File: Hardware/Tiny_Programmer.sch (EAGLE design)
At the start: 31 parts, among them Q1 16MHz, U1 ATTINY84, X1 USB-A-H

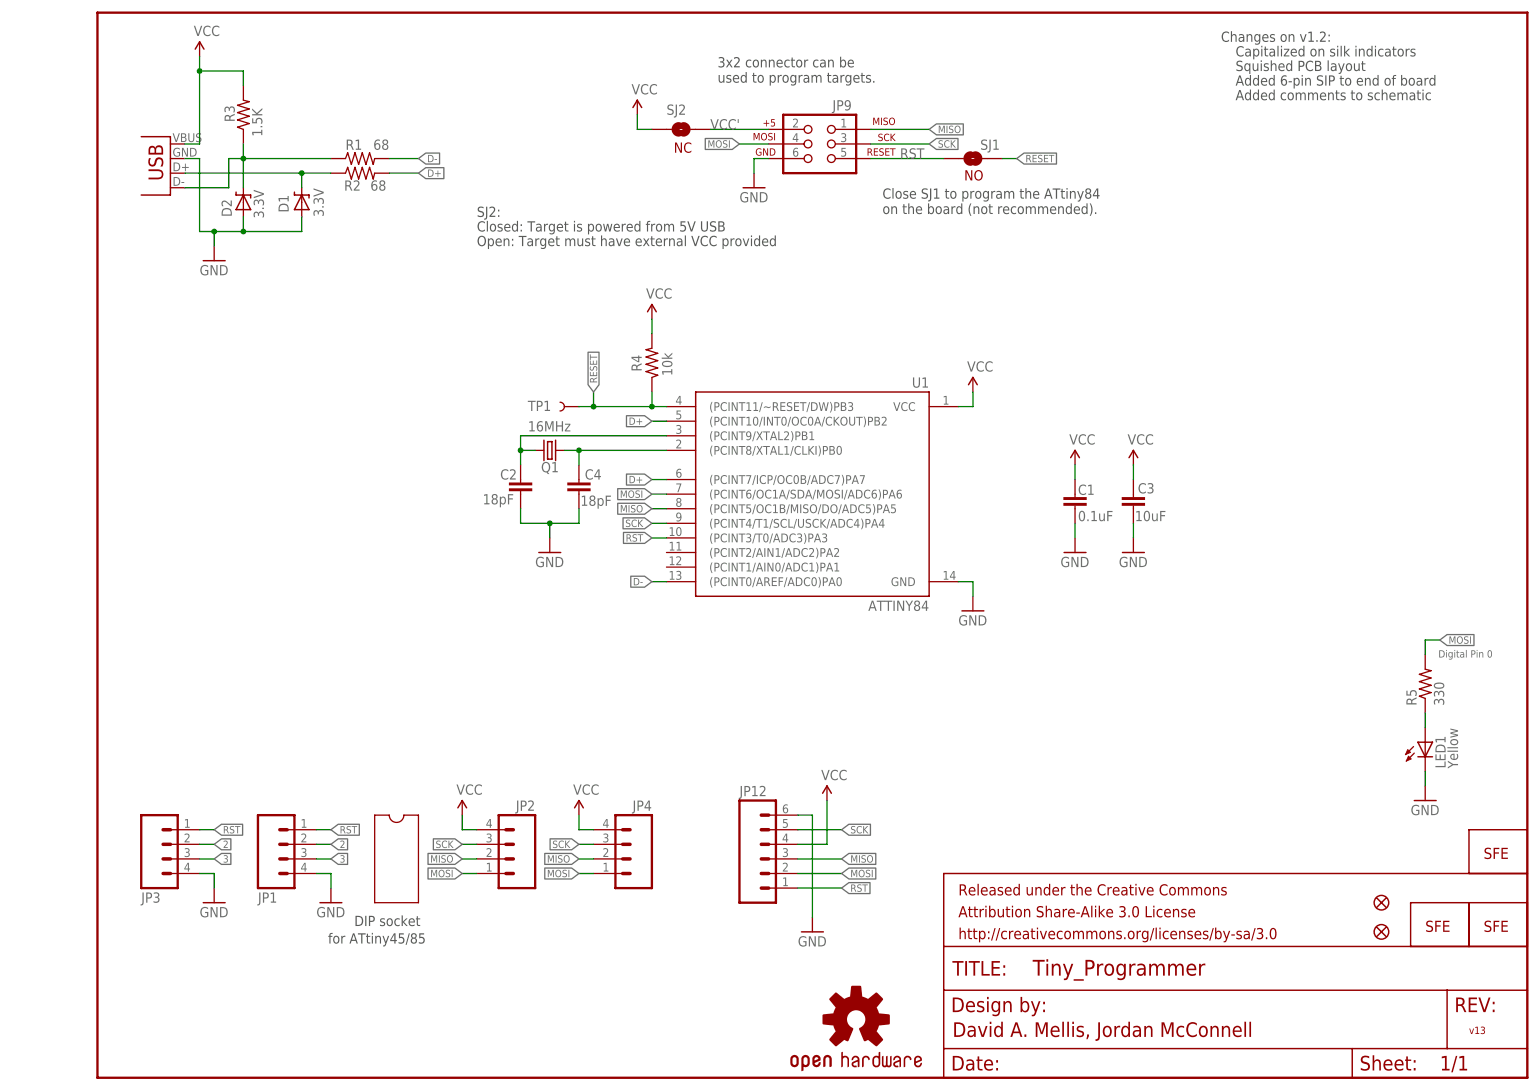
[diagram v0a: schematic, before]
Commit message: replace USB port, and redraw board
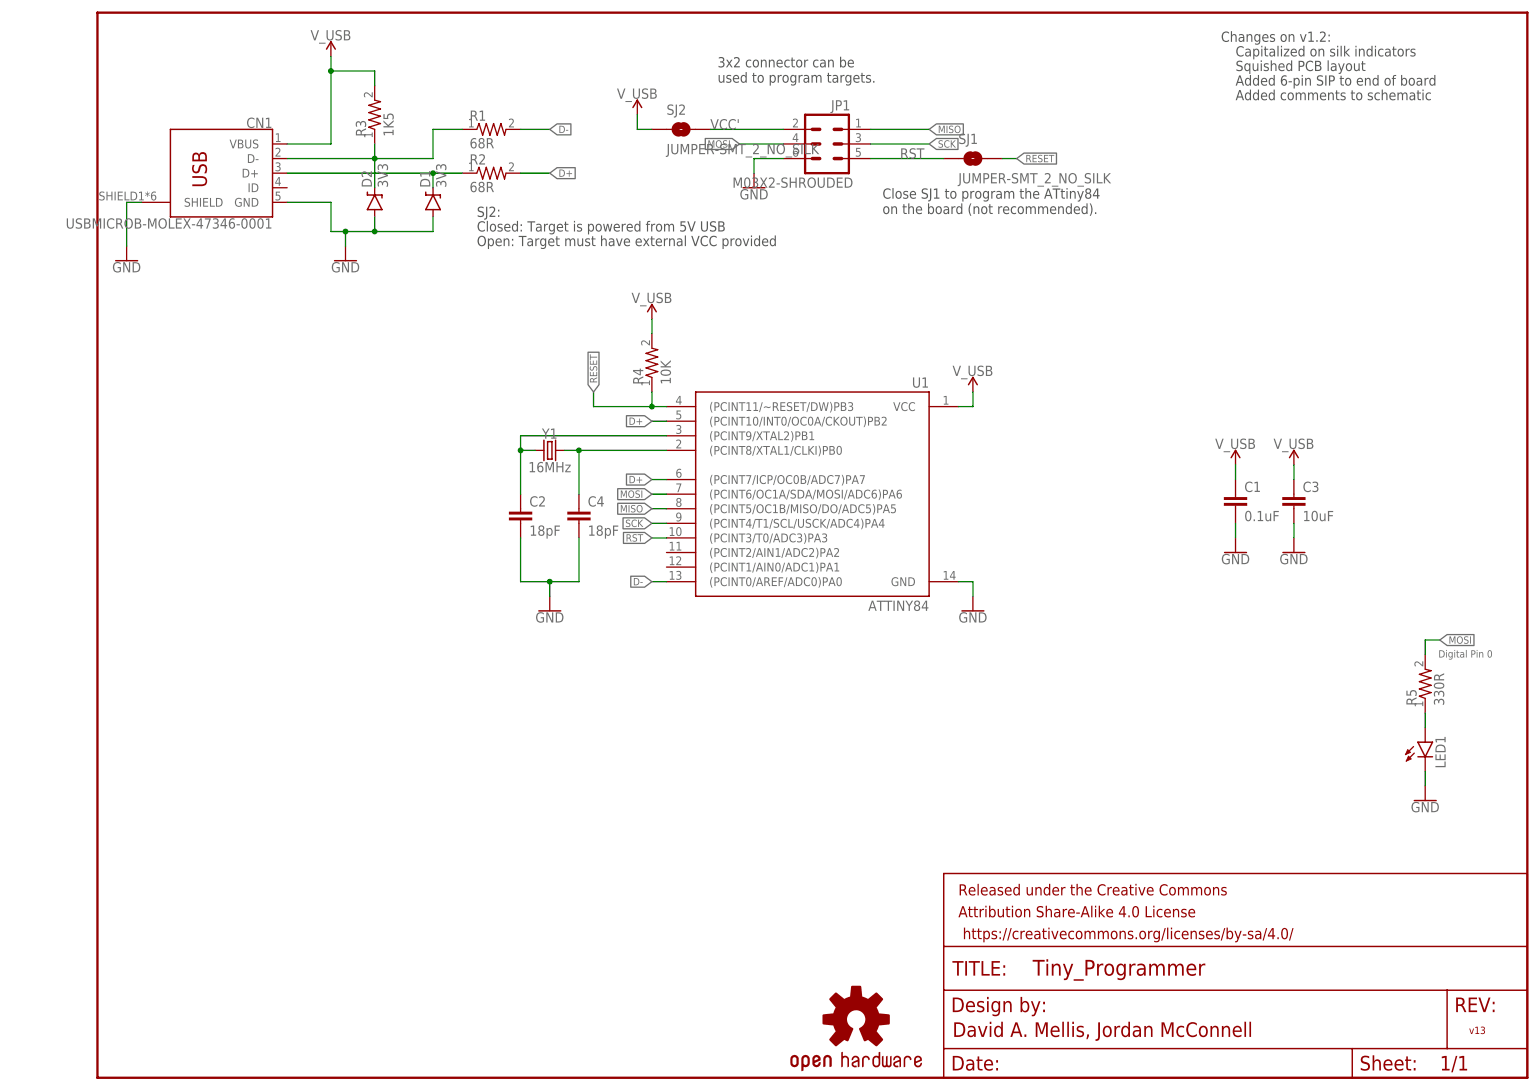
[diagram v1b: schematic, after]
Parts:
- removed JP11, JP6: LOGO-SFESK, SparkFun-Aesthetics:LOGO-SFESK
- removed JP12: (no value), SparkFun-Connectors:M06SIP
- removed JP2: (no value), SparkFun-Connectors:M04PTH
- removed JP3, JP4: (no value), SparkFun-Connectors:M04SMD_STRAIGHT_COMBO
- removed JP5: LOGO-SFENW2, SparkFun-Aesthetics:LOGO-SFENW2
- removed JP7, JP8: FIDUCIALUFIDUCIAL, SparkFun:FIDUCIALUFIDUCIAL
- removed JP9: AVR_SPI_PRG_6PTH, SparkFun-Connectors:AVR_SPI_PRG_6PTH
- removed Q1: 16MHz, SparkFun-FreqCtrl:CRYSTAL5X3
- removed TP1: TEST-POINT3, SparkFun-Passives:TEST-POINT3
- removed X1: USB-A-H, SparkFun-Connectors:USB-A-H
- added CN1: USBMICROB-MOLEX-47346-0001, Connectors:USBMICROB-MOLEX-47346-0001
- added Y1: 16MHz, SparkFun-Clocks:CRYSTAL-16MHZSMD-5X3.2
- C1, C2, C3, C4: device SparkFun-Passives:CAP0402-CAP -> Darryl-Capacitors:CAPACITOR-0603
- D1, D2: value 3.3V -> 3V3; device SparkFun-DiscreteSemi:DIODE-ZENER-BZT52 -> Darryl-DiscreteSemi:DIODE-ZENER-SOD-323
- JP1: value (none) -> M03X2-SHROUDED; device SparkFun-Connectors:M04PTH -> Darryl:M03X2-SHROUDED
- LED1: value Yellow -> (none); device SparkFun-LED:LED0603 -> Darryl:LED0603
- R1, R2: value 68 -> 68R; device SparkFun-Passives:RESISTOR0402-RES -> Darryl-Resistors:RESISTOR-0603
- R3: value 1.5K -> 1K5; device SparkFun-Passives:RESISTOR0402-RES -> Darryl-Resistors:RESISTOR-0603
- R4: value 10k -> 10K; device SparkFun-Passives:RESISTOR0402-RES -> Darryl-Resistors:RESISTOR-0603
- R5: value 330 -> 330R; device SparkFun-Passives:RESISTOR0402-RES -> Darryl-Resistors:RESISTOR-0603
- SJ1: value SOLDERJUMPERNO -> JUMPER-SMT_2_NO_SILK; device SparkFun-Passives:SOLDERJUMPERNO -> SparkFun-Jumpers:JUMPER-SMT_2_NO_SILK
- SJ2: value NC -> JUMPER-SMT_2_NO_SILK; device SparkFun-Passives:SOLDERJUMPERNC -> SparkFun-Jumpers:JUMPER-SMT_2_NO_SILK
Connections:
- removed net 2: JP1.2, JP3.2
- removed net 3: JP1.3, JP3.3
- removed net VCC: C1.1, C3.1, JP12.4, JP2.4, JP4.4, R3.2, R4.2, SJ2.1, U1.VCC, X1.GND
- new net V_USB: C1.1, C3.1, CN1.VBUS, R3.2, R4.2, SJ2.1, U1.VCC
- net GND: now also CN1.GND, CN1.SHIELD, JP1.6; no longer JP1.4, JP12.6, JP3.4, JP9.6, X1.VBUS
- net MISO: now also JP1.1; no longer JP12.3, JP2.2, JP4.2, JP9.1
- net MOSI: now also JP1.4; no longer JP12.2, JP2.1, JP4.1, JP9.4
- net N$1: now also CN1.D-; no longer X1.D+
- net N$2: now also CN1.D+; no longer X1.D-
- net N$3: now also Y1.1; no longer Q1.2
- net N$4: now also Y1.2; no longer Q1.1
- net RESET: now also SJ1.2; no longer SJ1.1, TP1.1
- net RST: now also JP1.5, SJ1.1; no longer JP1.1, JP12.1, JP3.1, JP9.5, SJ1.2
- net SCK: now also JP1.3; no longer JP12.5, JP2.3, JP4.3, JP9.3
- net VCC': now also JP1.2; no longer JP9.2
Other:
- note removed: "DIP socket"
- note removed: "NC"
- note removed: "NO"
- note removed: "for ATtiny45/85"
